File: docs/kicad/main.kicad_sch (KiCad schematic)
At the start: 7 parts, among them P1 Pololu_5V_Step_Down_Regulator, SW1 SW1

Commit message: Updating PCB to match schematic.
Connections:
- net +3V3: now also R1.2; no longer R1.1
- net RESET_DOWN: now also R1.1; no longer R1.2
- net SCL: now reaches F1.4 (SCL), MCU1.27 (SCL), MCU2.27 (SCL)
- net SDA: now reaches F1.5 (SDA), MCU1.28 (SDA), MCU2.28 (SDA)
- net BT_INT: now reaches MCU1.5 (A0), MCU2.5 (A0)
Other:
- moved on the sheet: R1
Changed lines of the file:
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@@
-    (stroke (width 0) (type default) (color 0 0 0 0))
-  )
-  (wire (pts (xy 52.07 35.56) (xy 52.07 38.1))
     (stroke (width 0) (type default) (color 0 0 0 0))
   )
@@
     (effects (font (size 1.27 1.27)) (justify left bottom))
   )
+  (label "SCL" (at 110.49 82.55 180)
+    (effects (font (size 1.27 1.27)) (justify right bottom))
+  )
   (label "M1PWM" (at 110.49 78.74 180)
     (effects (font (size 1.27 1.27)) (justify right bottom))
@@
     (effects (font (size 1.27 1.27)) (justify right bottom))
   )
+  (label "BT_INT" (at 49.53 44.45 0)
+    (effects (font (size 1.27 1.27)) (justify left bottom))
+  )
   (label "M3SLP" (at 49.53 55.88 0)
     (effects (font (size 1.27 1.27)) (justify left bottom))
   )
   (label "FIRE_DOWN" (at 110.49 59.69 180)
+    (effects (font (size 1.27 1.27)) (justify right bottom))
+  )
+  (label "SDA" (at 110.49 86.36 180)
     (effects (font (size 1.27 1.27)) (justify right bottom))
   )
@@
     (pin "1")
   )
-  (symbol (lib_id "power:GND") (at 52.07 38.1 0) (unit 1)
+  (symbol (lib_id "power:GND") (at 52.07 35.56 0) (unit 1)
     (in_bom yes) (on_board yes) (fields_autoplaced)
-    (property "Reference" "#PWR0109" (id 0) (at 52.07 44.45 0)
-      (effects (font (size 1.27 1.27)) hide)
-    )
-    (property "Value" "GND" (id 1) (at 52.07 42.6625 0))
-    (property "Footprint" "" (id 2) (at 52.07 38.1 0)
-      (effects (font (size 1.27 1.27)) hide)
-    )
-    (property "Datasheet" "" (id 3) (at 52.07 38.1 0)
+    (property "Reference" "#PWR0109" (id 0) (at 52.07 41.91 0)
+      (effects (font (size 1.27 1.27)) hide)
+    )
+    (property "Value" "GND" (id 1) (at 52.07 40.1225 0))
+    (property "Footprint" "" (id 2) (at 52.07 35.56 0)
+      (effects (font (size 1.27 1.27)) hide)
+    )
+    (property "Datasheet" "" (id 3) (at 52.07 35.56 0)
       (effects (font (size 1.27 1.27)) hide)
     )
@@
     (pin "9")
   )
-  (symbol (lib_id "Device:R_Small_US") (at 135.255 36.83 0) (unit 1)
+  (symbol (lib_id "Device:R_Small_US") (at 135.255 36.83 180) (unit 1)
     (in_bom yes) (on_board yes)
-    (property "Reference" "R1" (id 0) (at 136.9822 35.6616 0)
+    (property "Reference" "R1" (id 0) (at 133.5278 37.9984 0)
       (effects (font (size 1.27 1.27)) (justify left))
     )
-    (property "Value" "10K" (id 1) (at 136.9822 37.973 0)
+    (property "Value" "10K" (id 1) (at 133.5278 35.687 0)
       (effects (font (size 1.27 1.27)) (justify left))
     )

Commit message: Updating layout.
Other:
- moved on the sheet: P1, R1, SW1

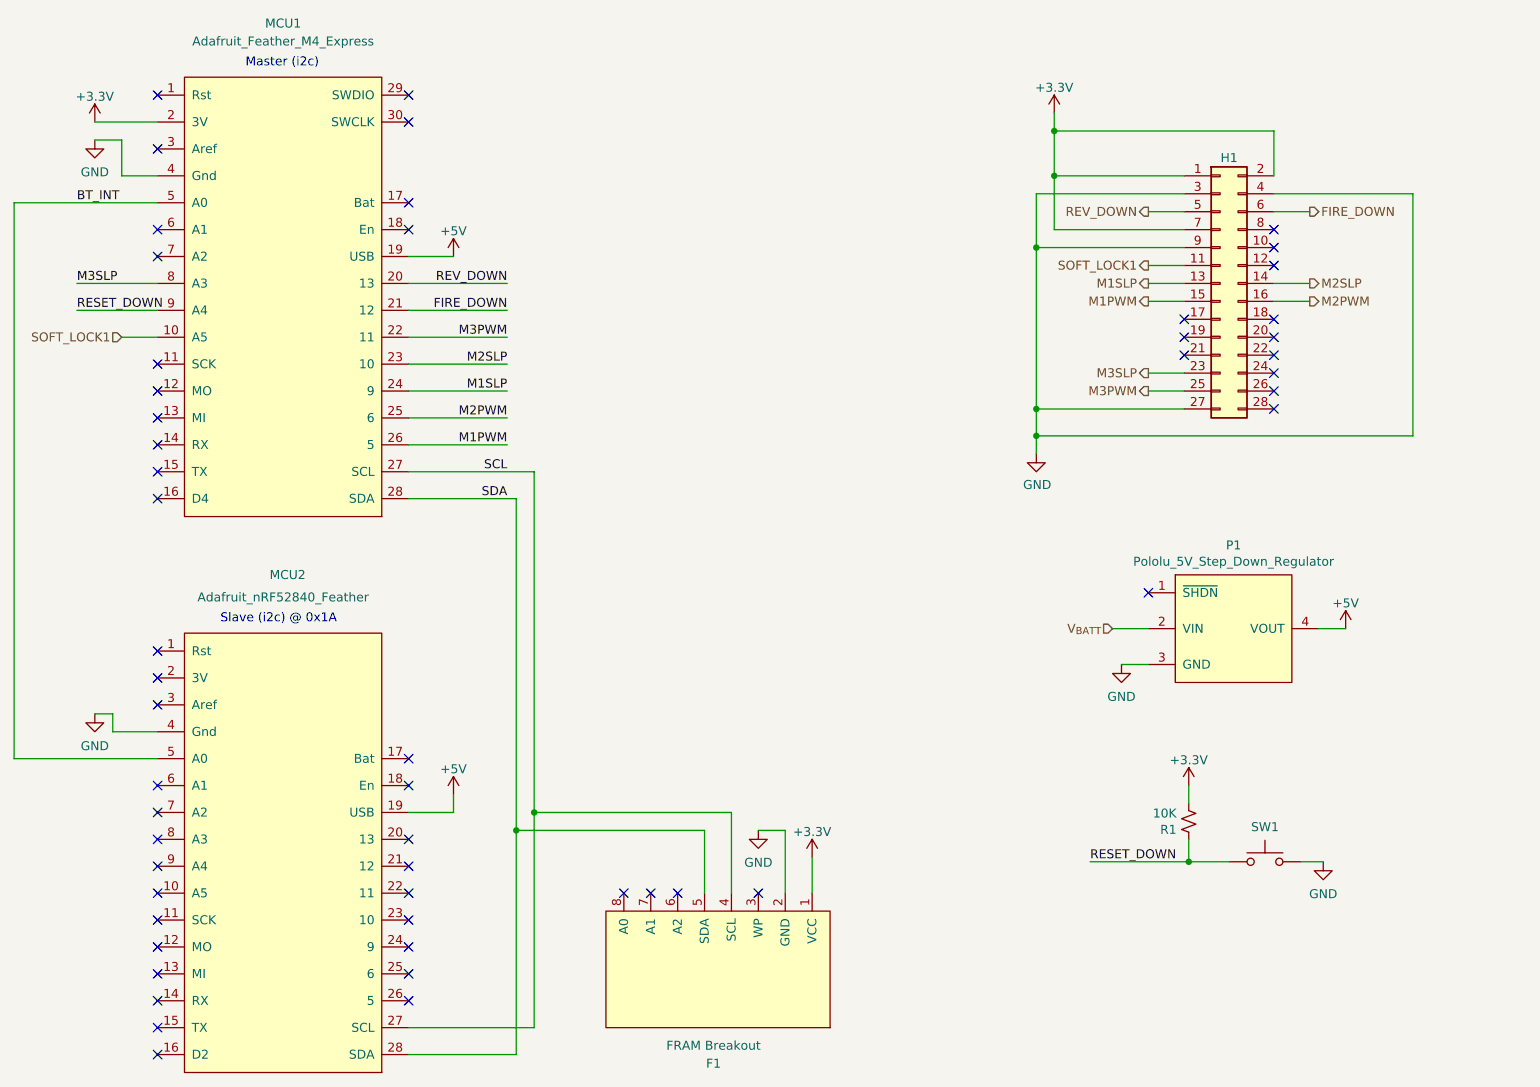
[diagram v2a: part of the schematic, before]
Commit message: Updating design to use SD card.
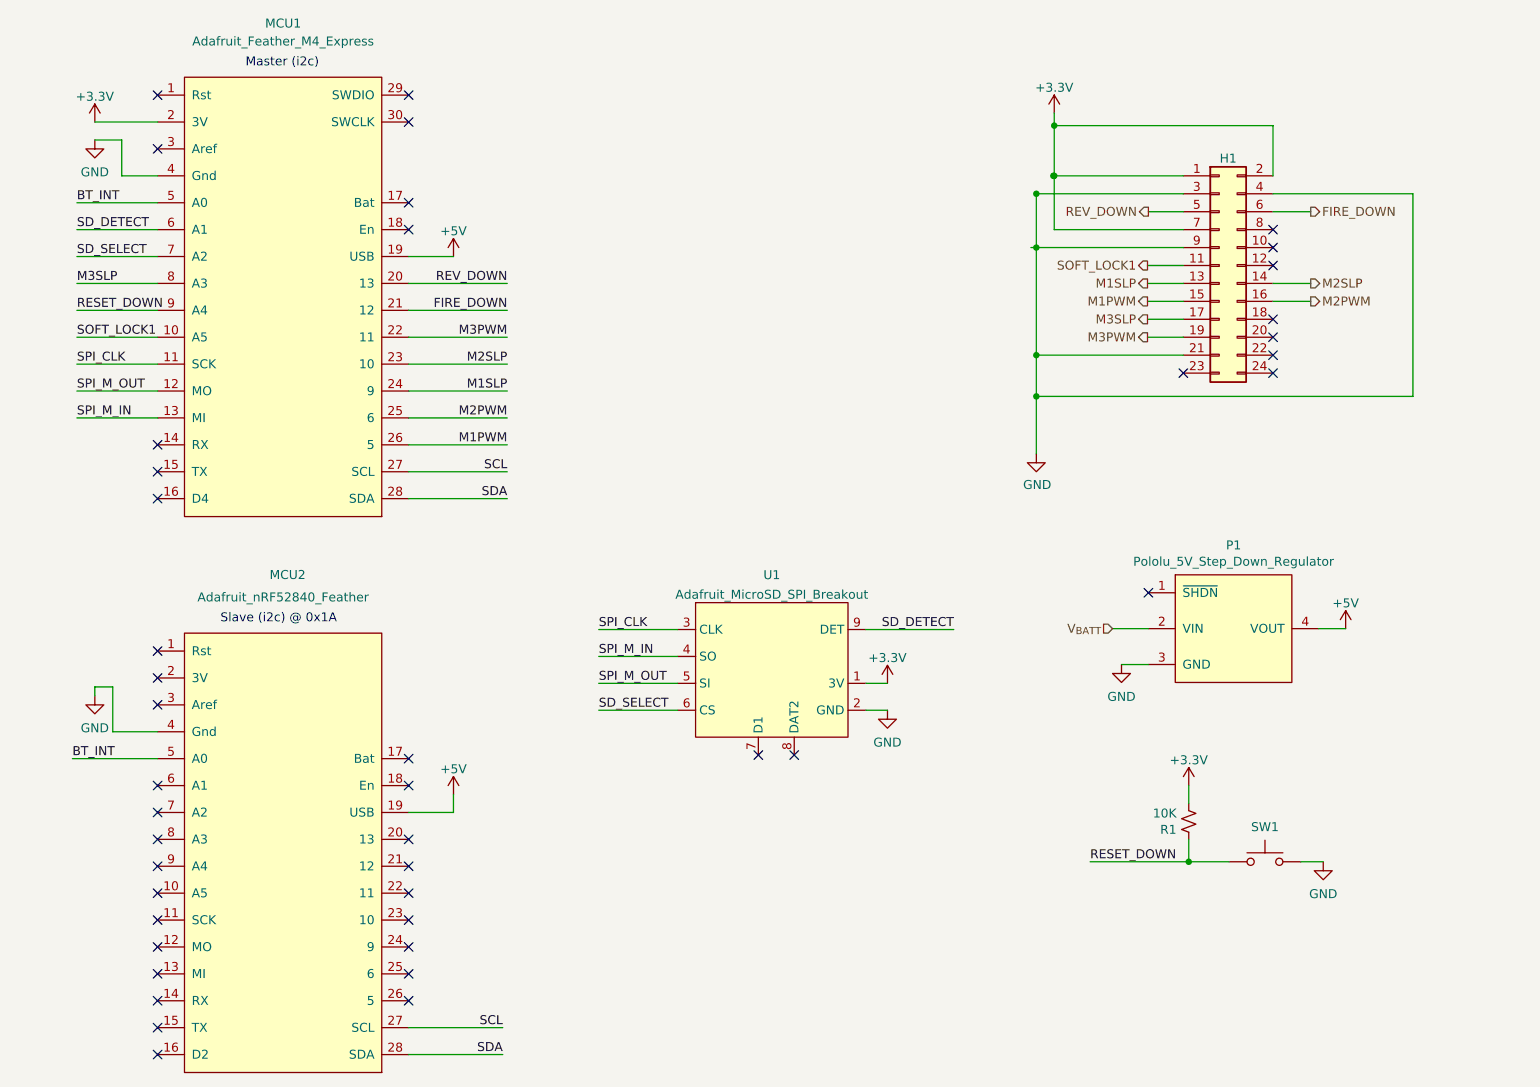
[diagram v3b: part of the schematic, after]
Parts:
- removed F1: FRAM Breakout, Adafruit:Adafruit_I2C_FRAM_Breakout, symbol Nemesis-Mod:Adafruit_I2C_FRAM_Breakout
- removed H1: (no value), Connector_PinHeader_2.54mm:PinHeader_2x14_P2.54mm_Vertical, symbol Connector_Generic:Conn_02x14_Odd_Even
- added H1: (no value), Connector_PinHeader_2.54mm:PinHeader_2x12_P2.54mm_Vertical, symbol Connector_Generic:Conn_02x12_Odd_Even
- added U1: Adafruit_MicroSD_SPI_Breakout, Adafruit:Adafruit_MicroSD_Breakout, symbol Nemesis-Mod:Adafruit_MicroSD_SPI_Breakout
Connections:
- net +3V3: now also H1.1 (Pin_1), H1.2 (Pin_2), H1.7 (Pin_7), U1.1 (3V)
- net FIRE_DOWN: now also H1.6 (Pin_6)
- net GND: now also H1.21 (Pin_21), H1.3 (Pin_3), H1.4 (Pin_4), H1.9 (Pin_9), U1.2 (GND)
- net M1PWM: now also H1.15 (Pin_15)
- net M1SLP: now also H1.13 (Pin_13)
- net M2PWM: now also H1.16 (Pin_16)
- net M2SLP: now also H1.14 (Pin_14)
- net M3PWM: now also H1.19 (Pin_19)
- net M3SLP: now also H1.17 (Pin_17)
- net REV_DOWN: now also H1.5 (Pin_5)
- net SOFT_LOCK1: now also H1.11 (Pin_11)
- net SPI_CLK: now reaches MCU1.11 (SCK)
- net SPI_CLK: now also U1.3 (CLK)
- net SPI_M_OUT: now reaches MCU1.12 (MO)
- net SPI_M_OUT: now also U1.5 (SI)
- net SPI_M_IN: now reaches MCU1.13 (MI)
- net SPI_M_IN: now also U1.4 (SO)
- net SD_DETECT: now reaches MCU1.6 (A1)
- net SD_DETECT: now also U1.9 (DET)
- net SD_SELECT: now reaches MCU1.7 (A2)
- net SD_SELECT: now also U1.6 (CS)
- no-connect marks 54 -> 43
